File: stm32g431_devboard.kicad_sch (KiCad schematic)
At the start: 1 part, among them U1 STM32G431CBTx

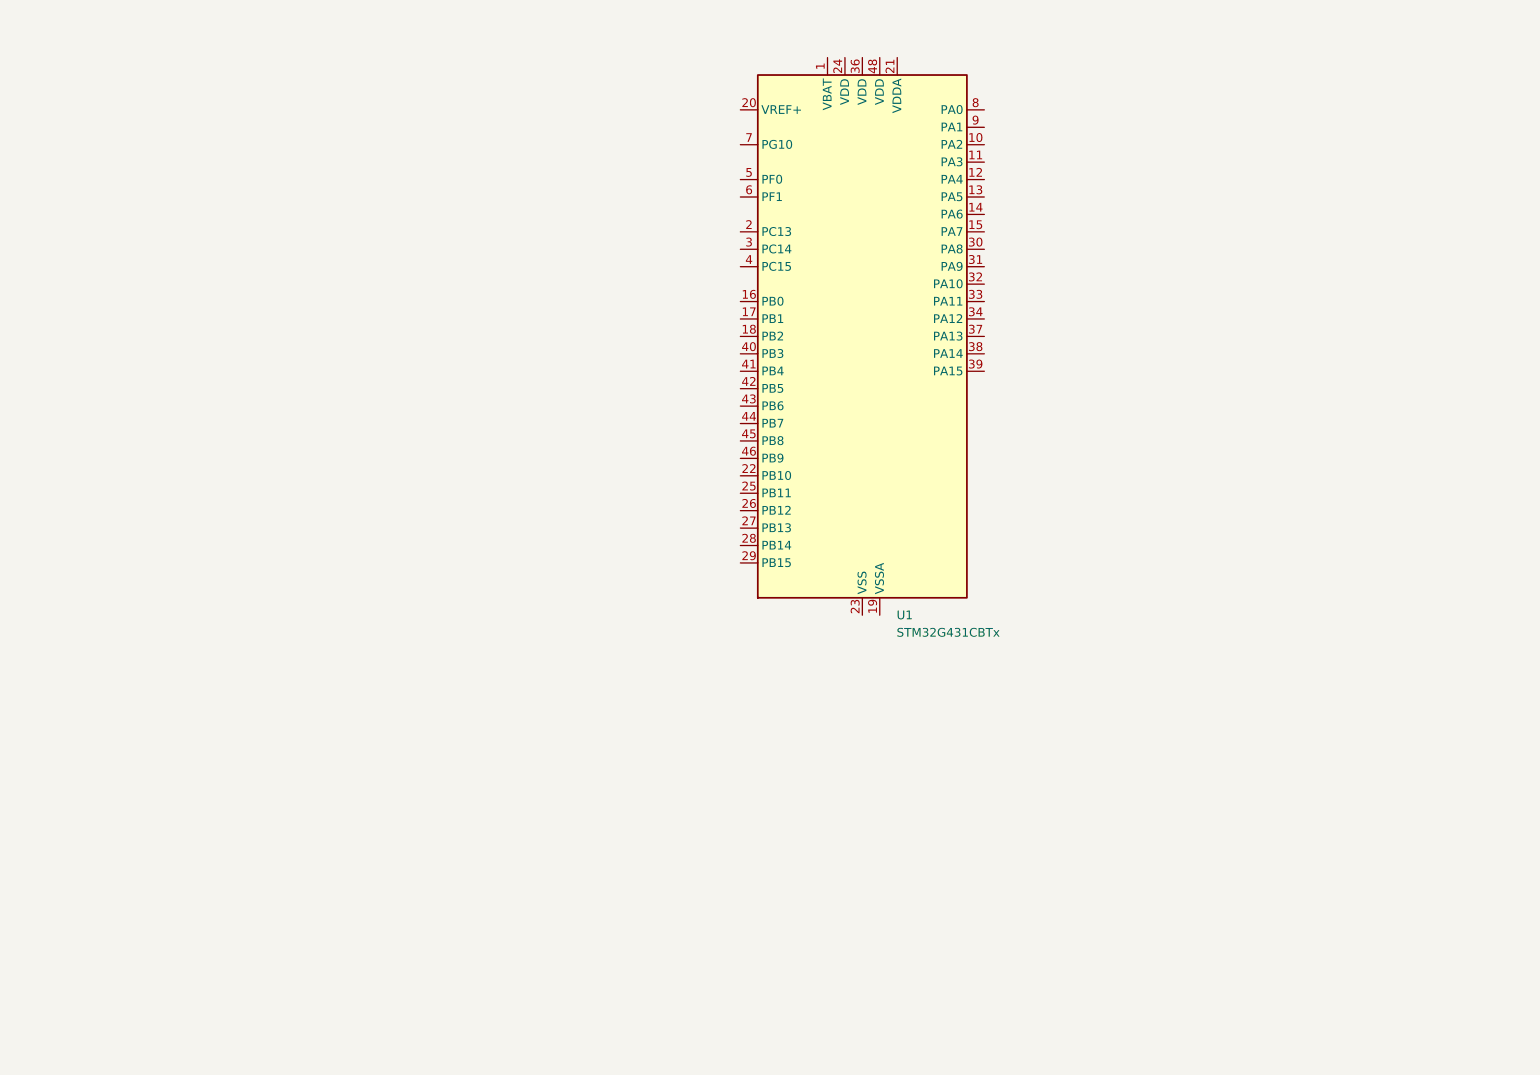
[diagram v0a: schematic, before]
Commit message: Add: Power Supply hierarchical sheet
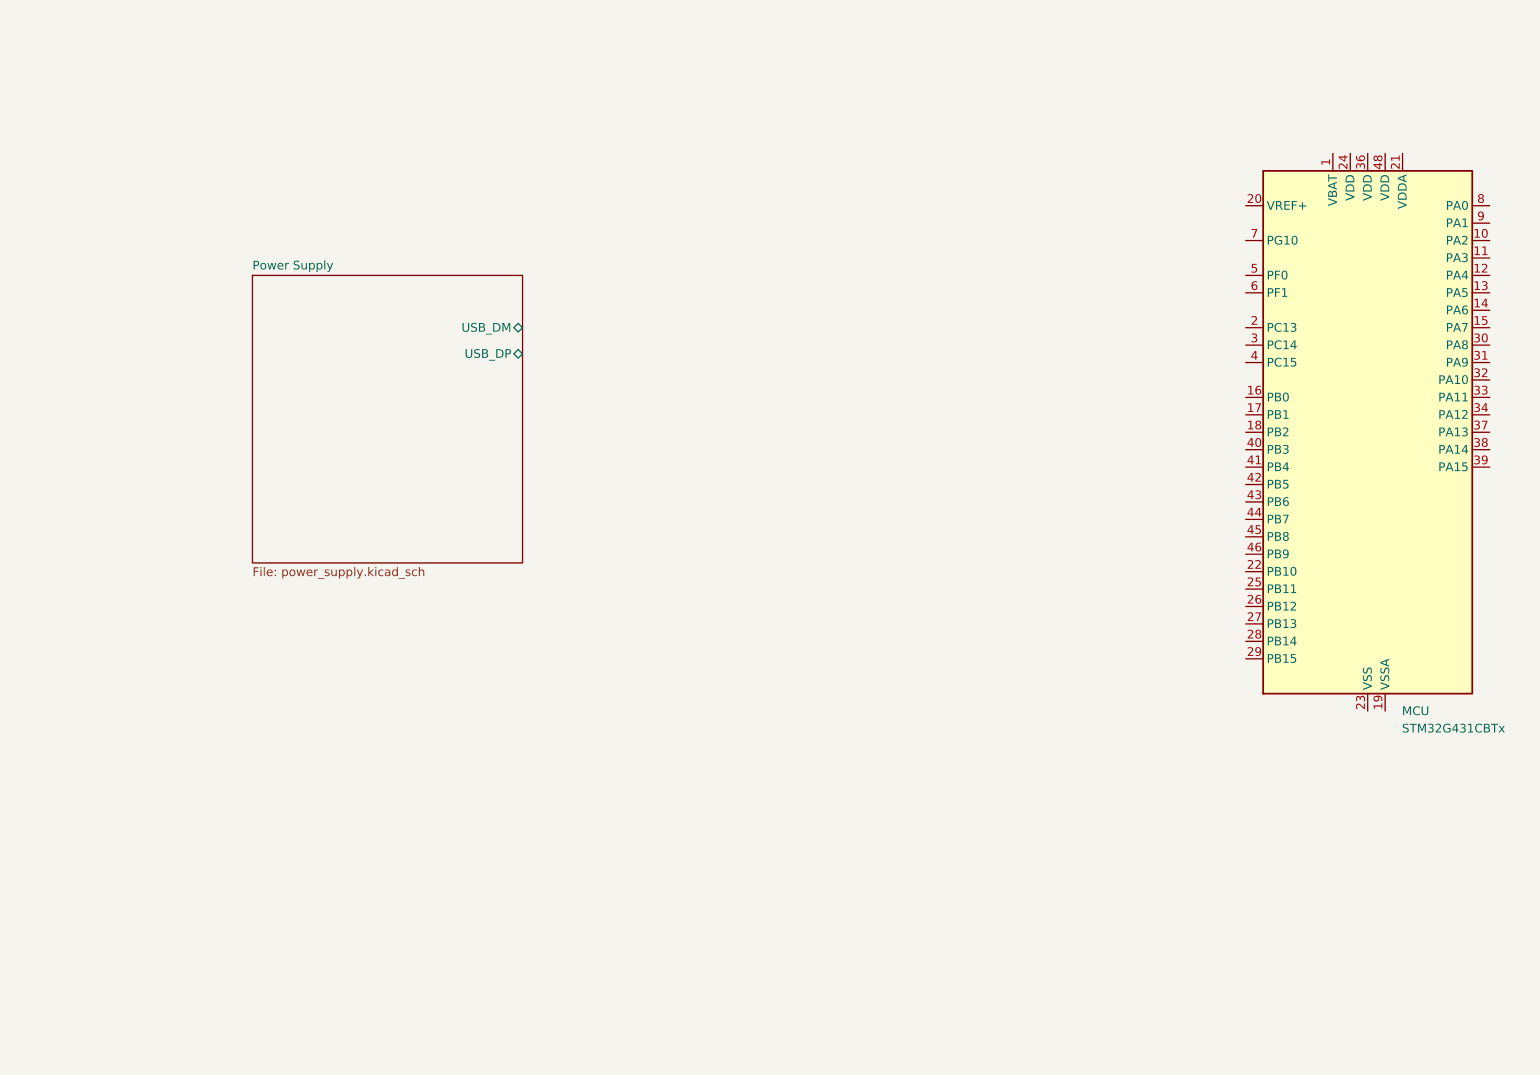
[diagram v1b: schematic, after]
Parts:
- renumbered U1 to MCU
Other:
- added sheet Power Supply (power_supply.kicad_sch)
- moved on the sheet: MCU
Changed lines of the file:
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@@
 	(symbol
 		(lib_id "MCU_ST_STM32G4:STM32G431CBTx")
-		(at 149.86 82.55 0)
+		(at 223.52 96.52 0)
 		(unit 1)
 		(body_style 1)
@@
 		(dnp no)
 		(fields_autoplaced yes)
-		(property "Reference" "U1"
-			(at 154.8463 123.19 0)
+		(property "Reference" "MCU"
+			(at 228.5063 137.16 0)
 			(show_name no)
 			(do_not_autoplace no)
@@
 		)
 		(property "Value" "STM32G431CBTx"
-			(at 154.8463 125.73 0)
+			(at 228.5063 139.7 0)
 			(show_name no)
 			(do_not_autoplace no)
@@
 		)
 		(property "Footprint" "Package_QFP:LQFP-48_7x7mm_P0.5mm"
-			(at 134.62 120.65 0)
+			(at 208.28 134.62 0)
 			(hide yes)
 			(show_name no)
@@
 		)
 		(property "Datasheet" "https://www.st.com/resource/en/datasheet/stm32g431cb.pdf"
-			(at 149.86 82.55 0)
+			(at 223.52 96.52 0)
 			(hide yes)
 			(show_name no)
@@
 		)
 		(property "Description" "STMicroelectronics Arm Cortex-M4 MCU, 128KB flash, 32KB RAM, 170 MHz, 1.71-3.6V, 38 GPIO, LQFP48"
-			(at 149.86 82.55 0)
+			(at 223.52 96.52 0)
 			(hide yes)
 			(show_name no)
@@
 			(project "stm32g431_devboard"
 				(path "/9df7c36b-7f78-4dc7-b3c3-09b2ad159e9d"
-					(reference "U1")
+					(reference "MCU")
 					(unit 1)
 				)
 			)
+		)
+	)
+	(sheet
+		(at 60.96 73.66)
+		(size 39.37 41.91)
+		(exclude_from_sim no)
+		(in_bom yes)
+		(on_board yes)
+		(dnp no)
+		(fields_autoplaced yes)
+		(stroke
+			(width 0.1524)
+			(type solid)
+		)
+		(fill
+			(color 0 0 0 0)
+		)
+		(property "Sheetname" "Power Supply"
+			(at 60.96 72.9484 0)
+			(show_name no)
+			(do_not_autoplace no)
+			(effects
+				(font
+					(size 1.27 1.27)
+				)
+				(justify left bottom)
+			)
+		)
+		(property "Sheetfile" "power_supply.kicad_sch"
+			(at 60.96 116.1546 0)
+			(show_name no)
+			(do_not_autoplace no)
+			(effects
+				(font
+					(size 1.27 1.27)
+				)
+				(justify left top)
+			)
+		)
+		(pin "USB_DM" bidirectional
+			(at 100.33 81.28 0)
+			(effects
+				(font
+					(size 1.27 1.27)
+				)
+				(justify right)
+			)
+		)
+		(pin "USB_DP" bidirectional
+			(at 100.33 85.09 0)
+			(effects
+				(font
+					(size 1.27 1.27)
+				)
+				(justify right)
+			)
+		)
+		(instances
+			(project "stm32g431_devboard"
+				(path "/9df7c36b-7f78-4dc7-b3c3-09b2ad159e9d"
+					(page "2")
+				)
+			)

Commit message: Complete MCU power, debug, and boot circuits; add scope doc
Schematic additions:
- Add second Schottky on USB VBUS for full diode-OR protection
- Wire VBAT, VSS, VSSA to power nets
- Add VDD decoupling: 3x 100nF + 1x 4.7uF bulk
- Add VDDA filter: ferrite bead + 1uF + 10nF
- Add VREF+ selector jumper with decoupling and external input
- Wire USB_DP/USB_DM to PA12/PA11 (corrected pinout)
- Add SWD 5-pin header on PA13/PA14/NRST
- Add reset button with 100nF noise cap
- Add BOOT0 button on PB8 with 10k pull-down

Project documentation:
- Add docs/scope.md locking v1 feature list and v2 candidates
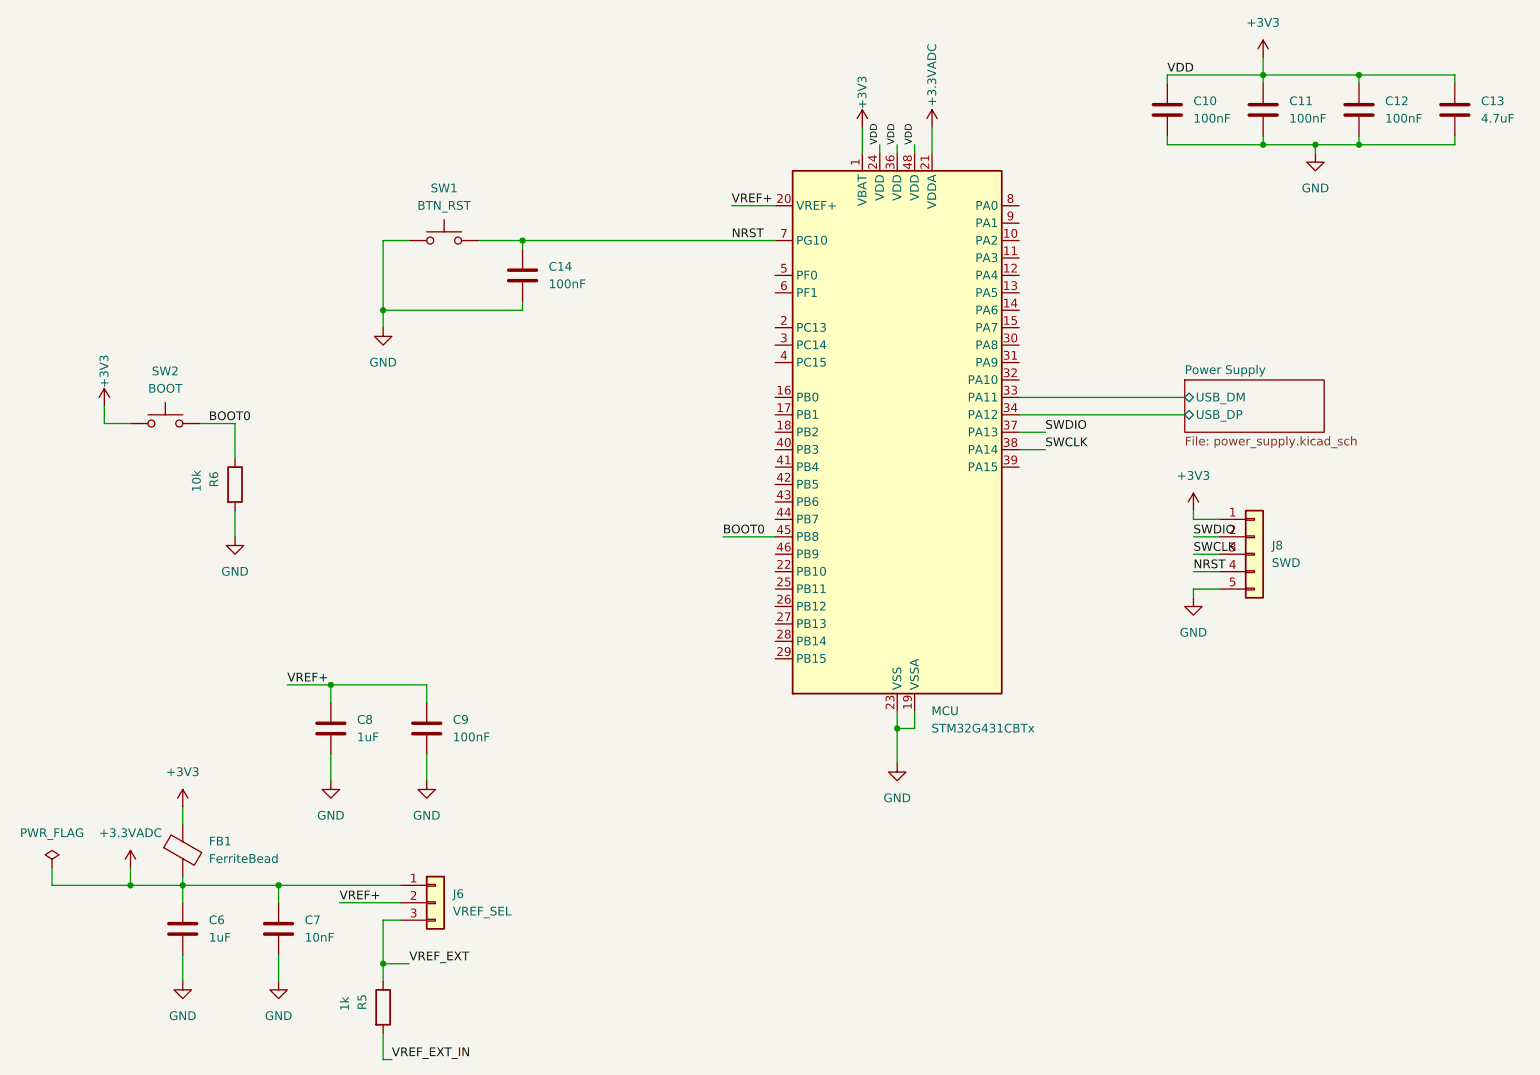
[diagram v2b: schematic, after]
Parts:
- added C10, C11, C12, C14, C9: 100nF, Capacitor_SMD:C_0603_1608Metric_Pad1.08x0.95mm_HandSolder, symbol Device:C
- added C13: 4.7uF, Capacitor_SMD:C_0603_1608Metric_Pad1.08x0.95mm_HandSolder, symbol Device:C
- added C6, C8: 1uF, Capacitor_SMD:C_0603_1608Metric_Pad1.08x0.95mm_HandSolder, symbol Device:C
- added C7: 10nF, Capacitor_SMD:C_0603_1608Metric_Pad1.08x0.95mm_HandSolder, symbol Device:C
- added FB1: FerriteBead, Inductor_SMD:L_0603_1608Metric_Pad1.05x0.95mm_HandSolder, symbol Device:FerriteBead
- added J6: VREF_SEL, Connector_PinHeader_2.54mm:PinHeader_1x03_P2.54mm_Vertical, symbol Connector_Generic:Conn_01x03
- added J8: SWD, Connector_PinHeader_2.54mm:PinHeader_1x05_P2.54mm_Vertical, symbol Connector_Generic:Conn_01x05
- added R5: 1k, Resistor_SMD:R_0603_1608Metric_Pad0.98x0.95mm_HandSolder, symbol Device:R
- added R6: 10k, Resistor_SMD:R_0603_1608Metric_Pad0.98x0.95mm_HandSolder, symbol Device:R
- added SW1: BTN_RST, Button_Switch_SMD:SW_SPST_TL3342, symbol Switch:SW_Push
- added SW2: BOOT, Button_Switch_SMD:SW_SPST_TL3342, symbol Switch:SW_Push
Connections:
- net Power Supply/USB_DM: now also MCU.33 (PA11)
- net Power Supply/USB_DP: now also MCU.34 (PA12)
- net +3V3: now reaches MCU.1 (VBAT)
- net +3V3: now also MCU.24 (VDD), MCU.36 (VDD), MCU.48 (VDD), C10.1, C11.1, C12.1, C13.1, FB1.1, J8.1 (Pin_1), SW2.1
- net GND: now reaches MCU.19 (VSSA)
- net GND: now also MCU.23 (VSS), MCU.35 (VSS), MCU.47 (VSS), C10.2, C11.2, C12.2, C13.2, C14.2, C6.2, C7.2, C8.2, C9.2, J8.5 (Pin_5), R6.2, SW1.1
- net VREF+: now reaches MCU.20 (VREF+)
- net VREF+: now also C8.1, C9.1, J6.2 (Pin_2)
- net +3.3VADC: now reaches MCU.21 (VDDA)
- net +3.3VADC: now also C6.1, C7.1, FB1.2, J6.1 (Pin_1)
- net SWDIO: now reaches MCU.37 (PA13)
- net SWDIO: now also J8.2 (Pin_2)
- net SWCLK: now reaches MCU.38 (PA14)
- net SWCLK: now also J8.3 (Pin_3)
- net BOOT0: now reaches MCU.45 (PB8)
- net BOOT0: now also R6.1, SW2.2
- net NRST: now reaches MCU.7 (PG10)
- net NRST: now also C14.1, J8.4 (Pin_4), SW1.2
- new net VREF_EXT: J6.3 (Pin_3), R5.1
- new net VREF_EXT_IN: R5.2
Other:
- moved on the sheet: MCU

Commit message: feat(schematic): complete v0.1 schematic for STM32G431 dev board
Three-sheet hierarchical design with clean ERC pass (0 errors, 0 warnings).

MCU (mcu.kicad_sch):
- STM32G431CBTx LQFP-48
- VDD decoupling (3× 100nF + 1× 4.7µF)
- VDDA filter via ferrite bead + 1µF + 10nF
- VREF+ selector jumper (internal +3V3A or external via 1kΩ series)
- SWD 5-pin header
- Reset button + 100nF noise cap
- BOOT0 button + 10kΩ pull-down

Power Supply (power_supply.kicad_sch):
- USB-C input (GCT USB4085) with 5.1kΩ CC pull-downs
- Diode-OR (SS14): USB + external JST 2-pin
- Dual LDO selector: AP2112K-3.3 and MCP1700-3302
- Current measurement jumper
- Power LEDs with disable jumpers
- USBLC6-2SC6 ESD protection on USB D+/D- with 100nF decoupling

GPIO Breakout (gpio_breakout.kicad_sch):
- 2× 20-pin headers, Black Pill style (40 pins total)
- Buses for PA, PB, PC, PF signal groups
- User LED on PB9 (470Ω current limit)
- User button on PB7 (10kΩ pull-up + 100nF debounce)
- UART header (USART2 on PA2/PA3) with 1kΩ series protection
- VREF_EXT_IN routed for external ADC reference
- NRST exposed for external reset access

USB and SWD signals routed individually; PA11-14 deliberately excluded
from the PA bus to keep USB/SWD pins isolated from the breakout.

Scope changes from initial plan:
- WS2812B RGB LEDs and 74AHCT125 level shifter moved to a separate
  follow-up board (Addressable RGB Demo)
- User LED moved from PA5 to PB9, user button moved from PB1 to PB7,
  freeing high-value ADC pins on the breakout
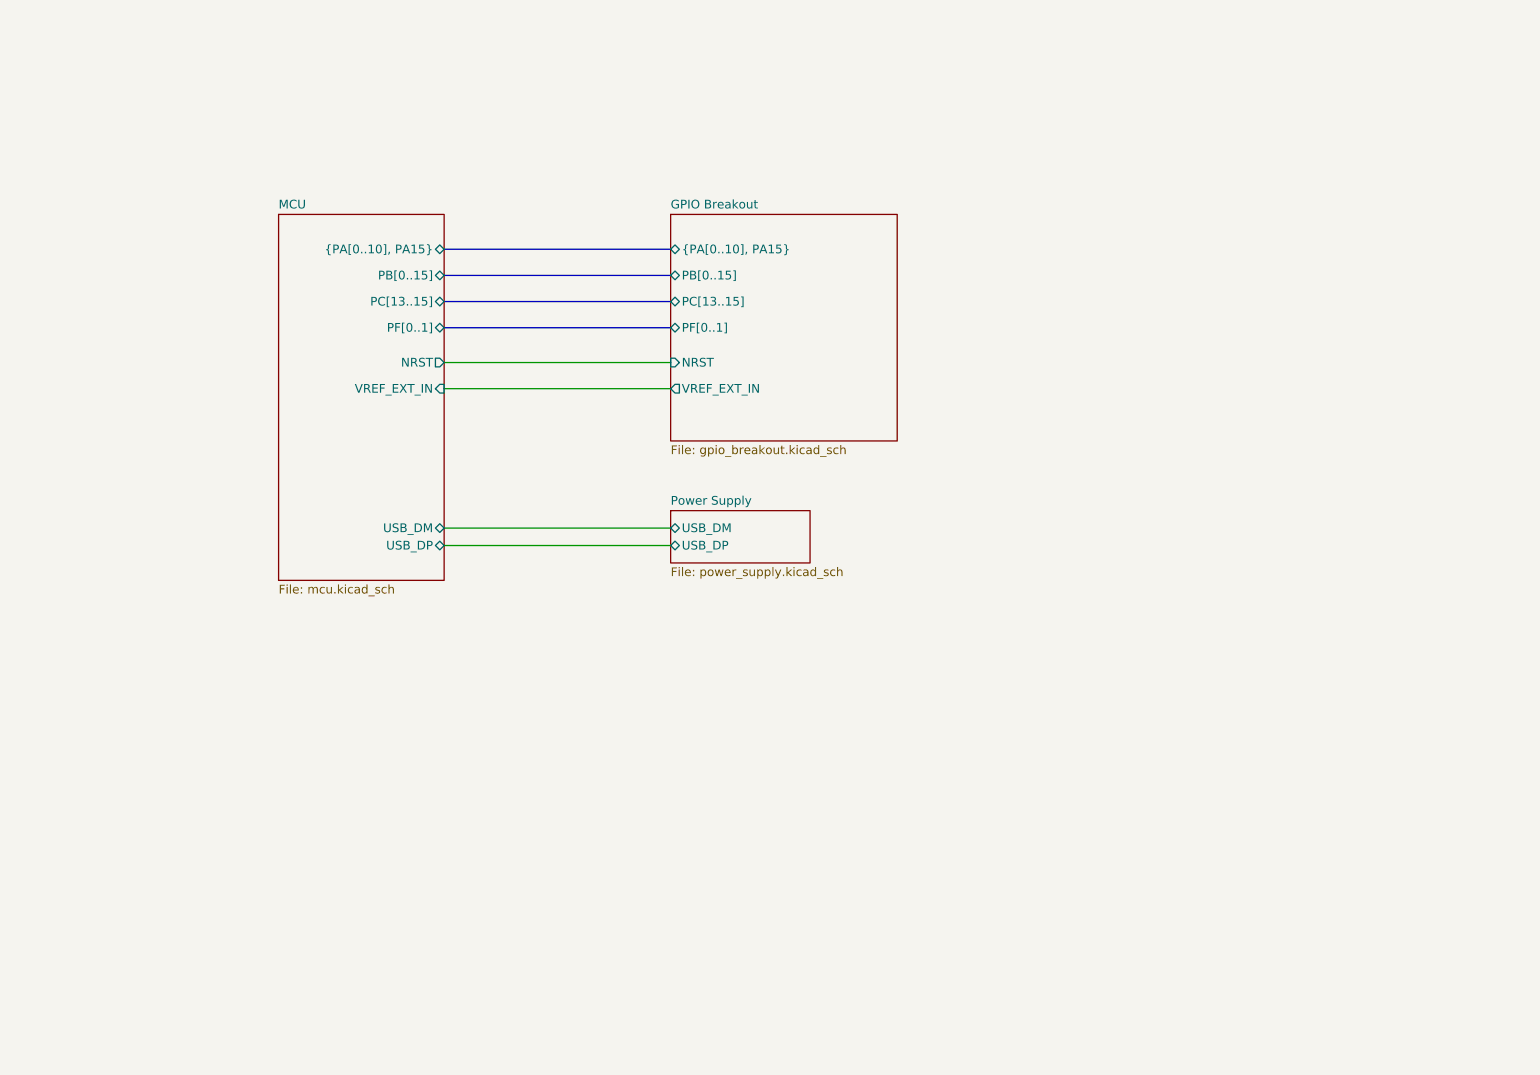
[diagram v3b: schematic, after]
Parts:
- removed C10, C11, C12, C14, C9: 100nF, Capacitor_SMD:C_0603_1608Metric_Pad1.08x0.95mm_HandSolder, symbol Device:C
- removed C13: 4.7uF, Capacitor_SMD:C_0603_1608Metric_Pad1.08x0.95mm_HandSolder, symbol Device:C
- removed C6, C8: 1uF, Capacitor_SMD:C_0603_1608Metric_Pad1.08x0.95mm_HandSolder, symbol Device:C
- removed C7: 10nF, Capacitor_SMD:C_0603_1608Metric_Pad1.08x0.95mm_HandSolder, symbol Device:C
- removed FB1: FerriteBead, Inductor_SMD:L_0603_1608Metric_Pad1.05x0.95mm_HandSolder, symbol Device:FerriteBead
- removed J6: VREF_SEL, Connector_PinHeader_2.54mm:PinHeader_1x03_P2.54mm_Vertical, symbol Connector_Generic:Conn_01x03
- removed J8: SWD, Connector_PinHeader_2.54mm:PinHeader_1x05_P2.54mm_Vertical, symbol Connector_Generic:Conn_01x05
- removed MCU: STM32G431CBTx, Package_QFP:LQFP-48_7x7mm_P0.5mm, symbol MCU_ST_STM32G4:STM32G431CBTx
- removed R5: 1k, Resistor_SMD:R_0603_1608Metric_Pad0.98x0.95mm_HandSolder, symbol Device:R
- removed R6: 10k, Resistor_SMD:R_0603_1608Metric_Pad0.98x0.95mm_HandSolder, symbol Device:R
- removed SW1: BTN_RST, Button_Switch_SMD:SW_SPST_TL3342, symbol Switch:SW_Push
- removed SW2: BOOT, Button_Switch_SMD:SW_SPST_TL3342, symbol Switch:SW_Push
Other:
- added sheet GPIO Breakout (gpio_breakout.kicad_sch)
- added sheet MCU (mcu.kicad_sch)
